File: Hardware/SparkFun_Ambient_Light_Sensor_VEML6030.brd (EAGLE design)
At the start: 25.4 x 25.4 mm, 25 parts, among them U1 VEML6030

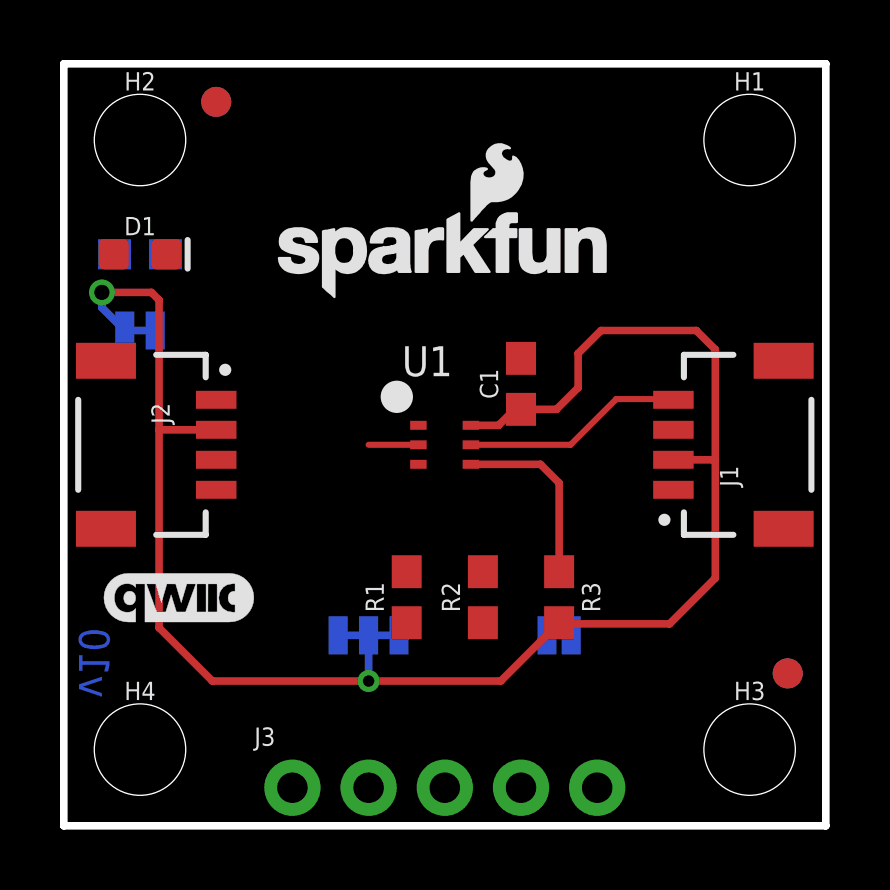
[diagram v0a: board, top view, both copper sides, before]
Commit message: Finishes tracework, adds 10k pull up resistor to interrupt pin, needs silk
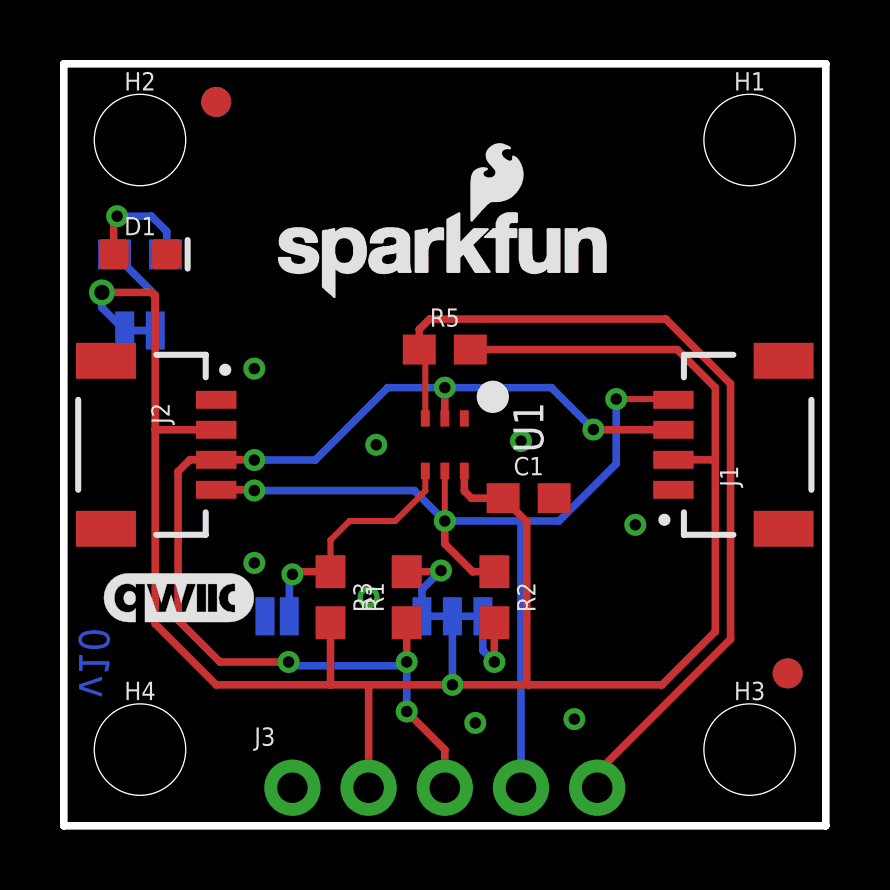
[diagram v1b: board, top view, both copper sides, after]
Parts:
- added R5: 10k, SparkFun-Resistors:0603
- moved JP2 9.42 mm to (7.11, 6.99)
- moved R3 7.62 mm to (8.89, 7.62)
- moved C1 3.82 mm to (15.5, 10.9), turned to 0 degrees
- moved JP3 2.87 mm to (13.0, 6.99)
- moved R2 0.38 mm to (14.4, 7.62), turned to 270 degrees
- turned U1 to 270 degrees
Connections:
- net !INT: now also R5.1
- net 3.3V: now also R5.2
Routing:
- net SDA: track 1.66 -> 38.6 mm, vias 0 -> 6
- net !INT: track 0.00 -> 29.8 mm
- net SCL: track 7.39 -> 32.0 mm, vias 0 -> 3
- net 3.3V: track 58.6 -> 71.3 mm
- net N$1: track 0.00 -> 3.96 mm, vias 0 -> 1
- net N$2: track 0.00 -> 3.10 mm
- net N$4: track 0.00 -> 2.99 mm, vias 0 -> 1
- net N$3: track 0.00 -> 2.95 mm, vias 0 -> 1
- net ADDR: track 6.16 -> 8.31 mm, vias 0 -> 1

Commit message: Adds silk to board for all things needing lables, adds text to jumpers in schematic,
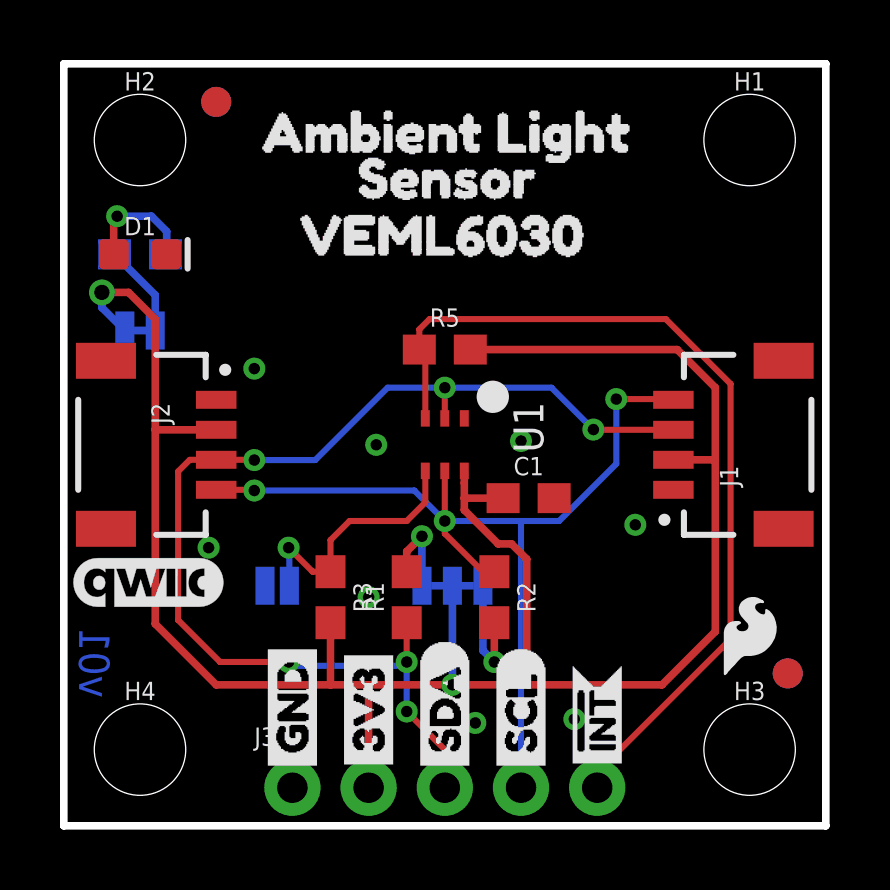
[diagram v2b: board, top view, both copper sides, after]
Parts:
- added U$10, U$5: (no value), Labels:SCL-[)
- added U$11, U$2: (no value), Labels:3V3-04
- added U$12: (no value), Labels:I_SUPER2_C-()-04
- added U$13: (no value), Labels:ADR-()
- added U$14: (no value), LED:LED0
- added U$15: (no value), Product Label:AMBIENT_LIGHT0
- added U$16: (no value), Product Label:SENSOR1
- added U$17: (no value), Product Label:VEML60302
- added U$18: (no value), SparkFun-Aesthetics:SFE_LOGO_FLAME_.1
- added U$3, U$8: (no value), Labels:GND-04
- added U$4, U$9: (no value), Labels:SDA-[)
- added U$6, U$7: (no value), Labels:INT#-[<
- moved FRAME1 49.5 mm to (-5.08, -11.4)
- moved LOGO1 1.48 mm to (13.5, 20.3), flipped to the bottom
- moved U$1 1.14 mm to (2.79, 8.13)
- moved JP2 1.02 mm to (7.11, 8.00)
- moved JP3 1.02 mm to (13.0, 8.00)
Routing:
- net 3.3V: track 71.3 -> 72.8 mm
- net N$4: track 2.99 -> 4.01 mm
- net ADDR: track 8.31 -> 9.07 mm
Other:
- board text added: "Elias Santistevan"
- board text added: "v01"
- board text removed: "v10"

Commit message: Updates polarity marker on VEML6030, adds VCC range to schematic, improves ground pour on the underside.
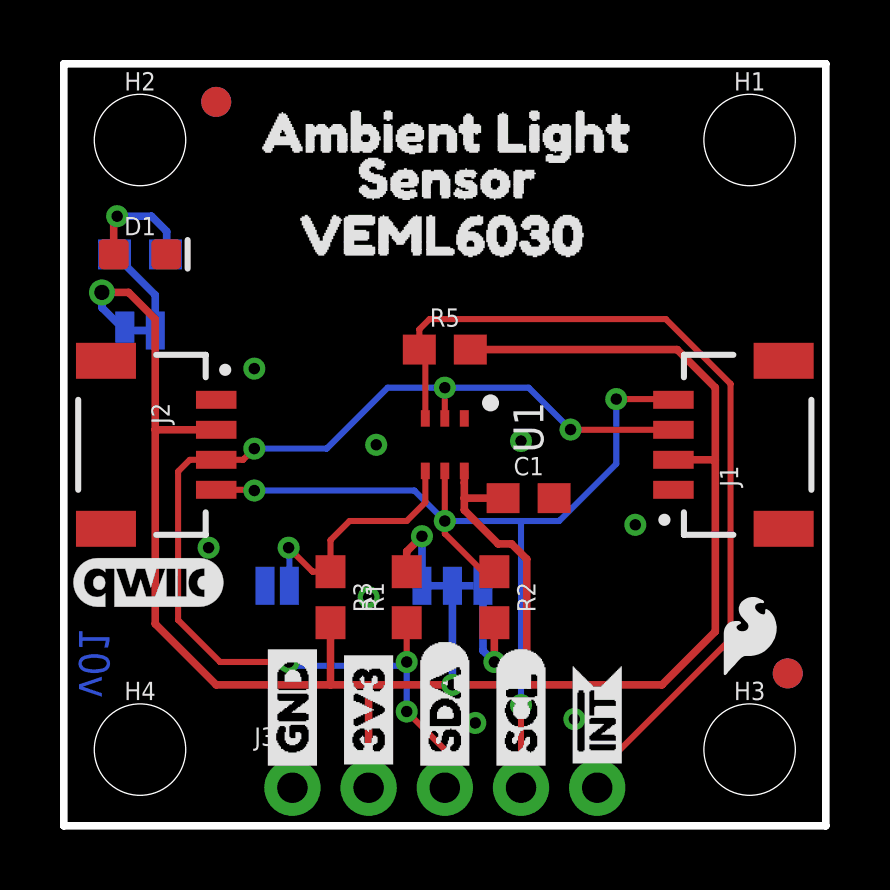
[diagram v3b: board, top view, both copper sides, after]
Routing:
- net SCL: vias 3 -> 4
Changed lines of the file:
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@@
 <drawing>
 <settings>
-<setting alwaysvectorfont="yes"/>
+<setting alwaysvectorfont="no"/>
 <setting verticaltext="up"/>
 </settings>
@@
 <via x="18.415" y="14.224" extent="1-16" drill="0.381"/>
 <wire x1="16.51" y1="10.16" x2="18.415" y2="12.065" width="0.2032" layer="16"/>
-<wire x1="15.24" y1="1.27" x2="15.24" y2="10.16" width="0.2032" layer="16"/>
 <wire x1="13.97" y1="8.47" x2="12.7" y2="9.74" width="0.2032" layer="1"/>
 <wire x1="12.7" y1="9.74" x2="12.7" y2="10.16" width="0.2032" layer="1"/>
 <wire x1="14.351" y1="8.47" x2="13.97" y2="8.47" width="0.2032" layer="1"/>
+<wire x1="15.24" y1="1.27" x2="15.24" y2="4.0259" width="0.2032" layer="1"/>
+<via x="15.24" y="4.0259" extent="1-16" drill="0.381"/>
+<wire x1="15.24" y1="4.0259" x2="15.24" y2="10.16" width="0.2032" layer="16"/>
 </signal>
 <signal name="SDA">
@@
 <via x="12.7" y="14.605" extent="1-16" drill="0.381"/>
 <wire x1="10.795" y1="14.605" x2="12.7" y2="14.605" width="0.2032" layer="16"/>
-<wire x1="5.08" y1="12.2" x2="6.342" y2="12.2" width="0.2032" layer="1"/>
-<wire x1="6.342" y1="12.2" x2="6.35" y2="12.192" width="0.2032" layer="1"/>
-<via x="6.35" y="12.192" extent="1-16" drill="0.381"/>
-<wire x1="6.35" y1="12.192" x2="8.382" y2="12.192" width="0.2032" layer="16"/>
-<wire x1="8.382" y1="12.192" x2="10.795" y2="14.605" width="0.2032" layer="16"/>
-<wire x1="12.7" y1="14.605" x2="16.256" y2="14.605" width="0.2032" layer="16"/>
-<wire x1="16.256" y1="14.605" x2="17.653" y2="13.208" width="0.2032" layer="16"/>
-<via x="17.653" y="13.208" extent="1-16" drill="0.381"/>
-<wire x1="17.653" y1="13.208" x2="17.661" y2="13.2" width="0.2032" layer="1"/>
-<wire x1="17.661" y1="13.2" x2="20.32" y2="13.2" width="0.2032" layer="1"/>
+<via x="6.35" y="12.573" extent="1-16" drill="0.381"/>
+<wire x1="6.35" y1="12.573" x2="8.763" y2="12.573" width="0.2032" layer="16"/>
+<wire x1="8.763" y1="12.573" x2="10.795" y2="14.605" width="0.2032" layer="16"/>
+<wire x1="12.7" y1="14.605" x2="15.494" y2="14.605" width="0.2032" layer="16"/>
+<wire x1="15.494" y1="14.605" x2="16.891" y2="13.208" width="0.2032" layer="16"/>
+<via x="16.891" y="13.208" extent="1-16" drill="0.381"/>
+<wire x1="16.891" y1="13.208" x2="16.899" y2="13.2" width="0.2032" layer="1"/>
+<wire x1="16.899" y1="13.2" x2="20.32" y2="13.2" width="0.2032" layer="1"/>
 <wire x1="5.08" y1="12.2" x2="4.199" y2="12.2" width="0.2032" layer="1"/>
 <wire x1="4.199" y1="12.2" x2="3.81" y2="11.811" width="0.2032" layer="1"/>
@@
 <wire x1="11.43" y1="5.461" x2="11.43" y2="6.77" width="0.2032" layer="1"/>
 <wire x1="11.43" y1="3.81" x2="11.43" y2="5.461" width="0.2032" layer="16"/>
+<wire x1="5.08" y1="12.2" x2="5.977" y2="12.2" width="0.2032" layer="1"/>
+<wire x1="5.977" y1="12.2" x2="6.35" y2="12.573" width="0.2032" layer="1"/>
 </signal>
 <signal name="N$1">
@@
 <wire x1="12.05" y1="10.78" x2="11.43" y2="10.16" width="0.2032" layer="1"/>
 <wire x1="11.43" y1="10.16" x2="9.525" y2="10.16" width="0.2032" layer="1"/>
-<wire x1="7.5184" y1="8.001" x2="7.5184" y2="8.2804" width="0.254" layer="16"/>
 <wire x1="8.89" y1="8.47" x2="8.294" y2="8.47" width="0.2032" layer="1"/>
 <wire x1="8.294" y1="8.47" x2="7.493" y2="9.271" width="0.2032" layer="1"/>
